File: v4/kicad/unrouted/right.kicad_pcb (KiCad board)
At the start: 2 copper layers, 160 x 118.6 mm, 72 parts

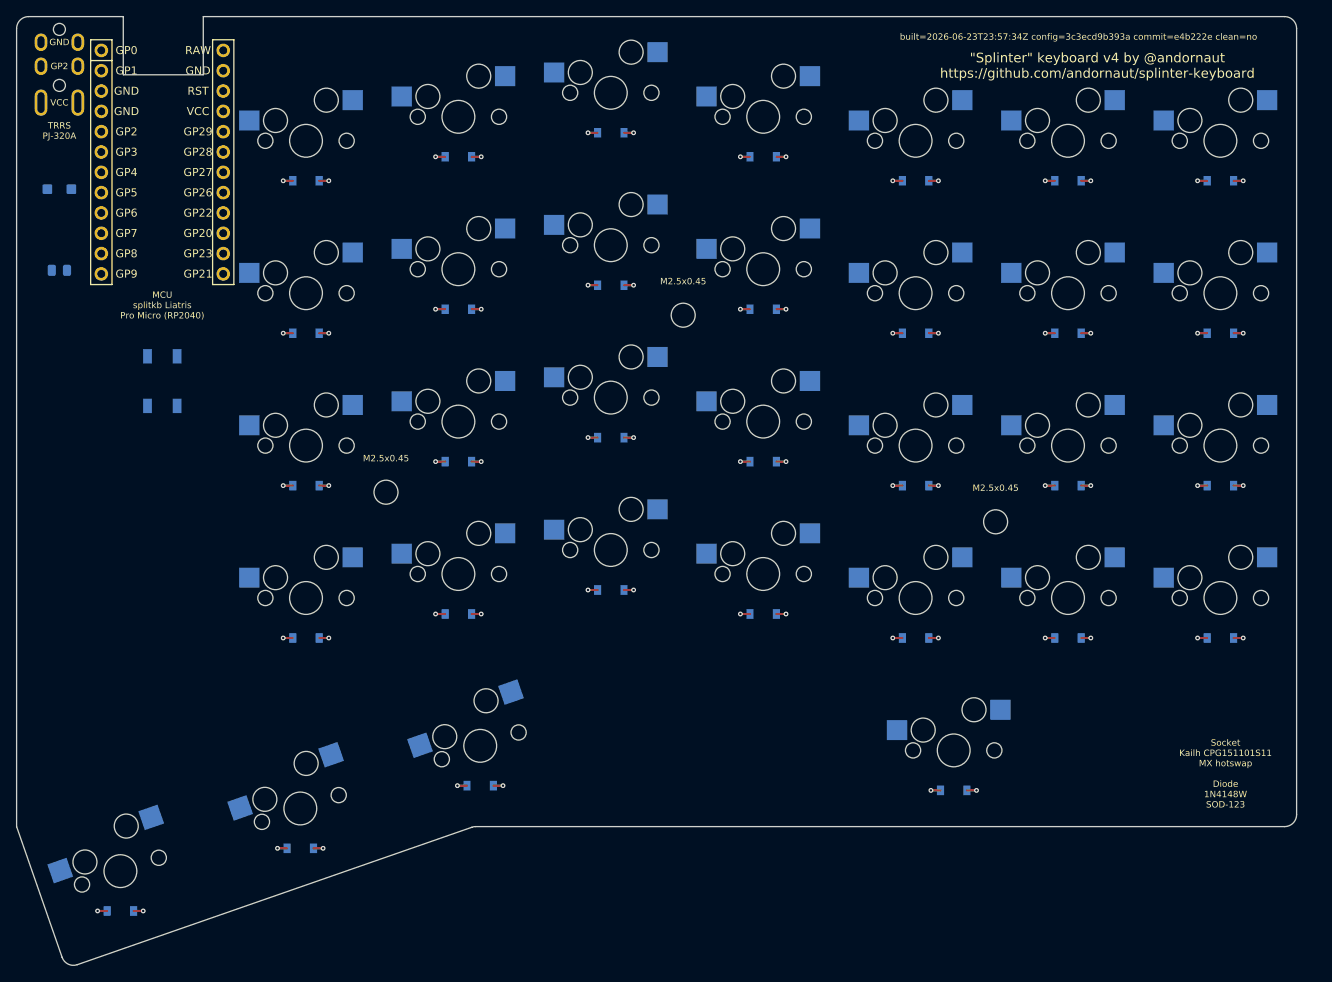
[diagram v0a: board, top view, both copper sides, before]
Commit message: v4: front-relative raw_pin_column, left-half nets on the partner pins
mcu_liatris now takes raw_pin_column: front_left | front_right instead of
left | right. The values name the PCB front because the MCU mounts on the
back, so the natural way to hold the board reverses the columns and the
bare left/right spelling silently assumed a frame. A stale left/right value
is rejected rather than reinterpreted.

The left half's matrix nets move to their socket-row partners (P4 -> P19,
P5 -> P18, and so on) so the net names and the silk labels name the pin
each net actually reaches. P2 stays put: QMK has one split.serial.pin, so
both halves must share it.

mcu_y seats the footprint body outline flush with the board top edge.

Regenerates unrouted/. routed/ is deliberately untouched and still carries
the wiring the boards were fabricated with, so validate:provenance and
validate:firmware both report it stale until it is re-routed.
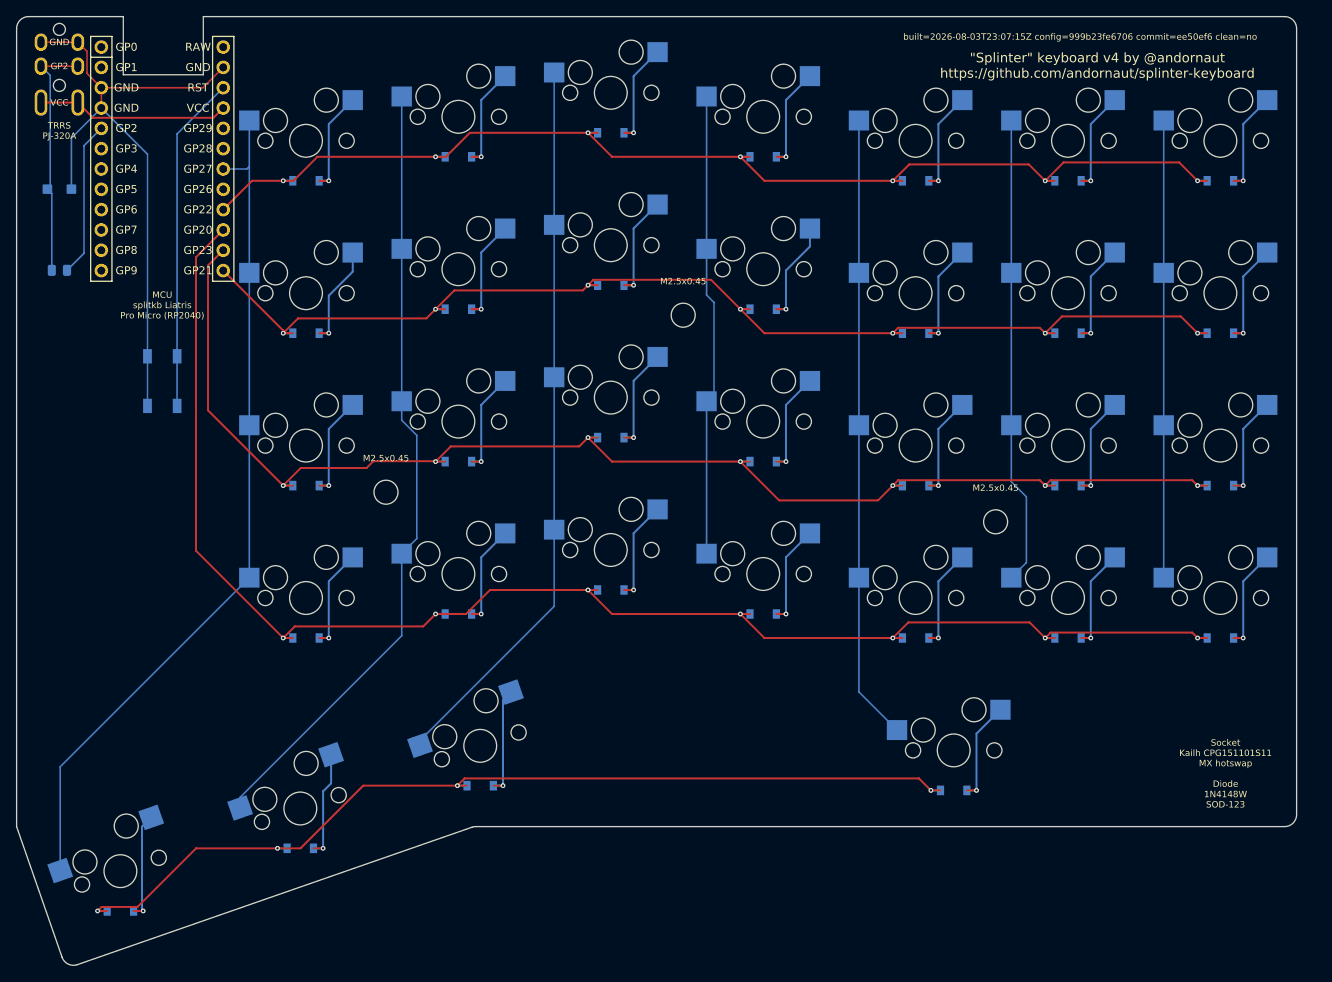
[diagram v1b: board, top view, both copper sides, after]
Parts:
- moved MCU1 0.42 mm to (148.5, 105.8)
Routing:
- net P14: track 16.8 -> 194.0 mm
- net P16: track 16.8 -> 172.9 mm
- net P10: track 16.8 -> 149.9 mm
- net P15: track 16.8 -> 146.3 mm
- net P9: track 9.60 -> 120.0 mm
- net P19: track 0.00 -> 106.9 mm
- net P8: track 0.00 -> 98.9 mm
- net P7: track 0.00 -> 91.0 mm
- net GND: track 0.00 -> 81.6 mm
- net P5: track 0.00 -> 78.2 mm
- net P4: track 0.00 -> 58.7 mm
- net P6: track 0.00 -> 57.9 mm
- net P3: track 0.00 -> 57.1 mm
- net RST: track 0.00 -> 42.2 mm
- net DATA_RAW: track 0.00 -> 31.0 mm
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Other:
- board text added: "built=2026-08-03T23:07:15Z config=999b23fe6706 commit=ee50ef6 clean=no"
- board text removed: "built=2026-06-23T23:57:34Z config=3c3ecd9b393a commit=e4b222e clean=no"

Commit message: v4: re-route both halves for the mirrored left-half pin mapping
Both halves are routed against the current config: the left half's matrix
nets on their MCU socket-row partners, and the MCU seated at the new mcu_y.
routed/ is re-derived from unrouted/ with the GND pour and teardrops (281
left, 296 right).

validate:provenance, validate:firmware, the fab DRC gate and validate:fab
all pass on all four boards. The routed/ .kicad_dru files land here for the
first time: apply-project-settings writes them per tier now.
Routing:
- net P3: track 57.1 -> 243.2 mm, vias 0 -> 1
- net P4: track 58.7 -> 225.0 mm, vias 0 -> 1
- net P5: track 78.2 -> 223.2 mm, vias 0 -> 1
- net P6: track 57.9 -> 183.2 mm, vias 0 -> 1
- net P7: track 91.0 -> 181.1 mm, vias 0 -> 1
- net P9: track 120.0 -> 194.2 mm
- net P8: track 98.9 -> 171.6 mm, vias 0 -> 1
- net P10: track 149.9 -> 142.5 mm
- net P15: track 146.3 -> 139.7 mm
- net P14: track 194.0 -> 190.6 mm
- net P16: track 172.9 -> 169.9 mm
- net mirror_five_mod: track 14.6 -> 13.2 mm, vias 1 -> 0
- net dash_upper: track 13.7 -> 12.5 mm, vias 1 -> 0
- net dash_num: track 13.7 -> 12.5 mm, vias 1 -> 0
- net dash_lower: track 13.7 -> 12.5 mm, vias 1 -> 0
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
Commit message: v4: strip the copper no route uses, in the pipeline
scripts/cleanup-tracks.py deletes dangling tracks and the vias they
strand, tracks buried in a pad of their own net, tracks laid over each
other, vias duplicating a via or a plated through-hole pad, and teardrops
left decorating nothing, then merges the segments an edit split.
copy:unrouted-to-routed runs it on each master after the GND pour, so the
fab source is cleaned every build. The working boards in unrouted/ keep
that copper, since a later reroute may pick it up.

scripts/pcb_copper.py holds the point-level connectivity test the cleanup
shares with add-gnd-zone.py, which now leaves the copper about to be
stripped out of its pour-layer score.

add-keepout-zones.py: weld the Edge.Cuts gap a stripped degenerate shape
leaves. KiCad closes a sub-micron gap silently but KiKit's ring
extraction matches endpoints exactly and aborts on it. One shape is
stripped per pass, because a weld moves the endpoints of the shapes still
to be tested.

Routed masters re-synced: DRC clean, 0 unconnected items, teardrops
unchanged (281 left, 296 right).
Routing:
- net P16: track 169.9 -> 178.3 mm
- net P15: track 139.7 -> 148.1 mm
- net P14: track 190.6 -> 199.0 mm
- net P10: track 142.5 -> 150.9 mm
- net P9: track 194.2 -> 199.0 mm
- net mirror_five_mod: track 13.2 -> 15.6 mm, vias 0 -> 1
- net P8: track 171.6 -> 169.5 mm
- net GND: track 82.0 -> 80.5 mm
- net dash_upper: track 12.5 -> 13.7 mm, vias 0 -> 1
- net dash_num: track 12.5 -> 13.7 mm, vias 0 -> 1
- net dash_lower: track 12.5 -> 13.7 mm, vias 0 -> 1
- net dash_home: track 12.5 -> 13.7 mm, vias 0 -> 1
- net zero_upper: track 12.5 -> 13.7 mm, vias 0 -> 1
- net zero_num: track 12.5 -> 13.7 mm, vias 0 -> 1
- net zero_lower: track 12.5 -> 13.7 mm, vias 0 -> 1
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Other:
- outline, holes or cut-outs redrawn
- board text added: "built=2026-08-04T01:57:26Z config=22a41bff1337 commit=3b96b62 clean=no"
- board text removed: "built=2026-08-03T23:07:15Z config=999b23fe6706 commit=ee50ef6 clean=no"

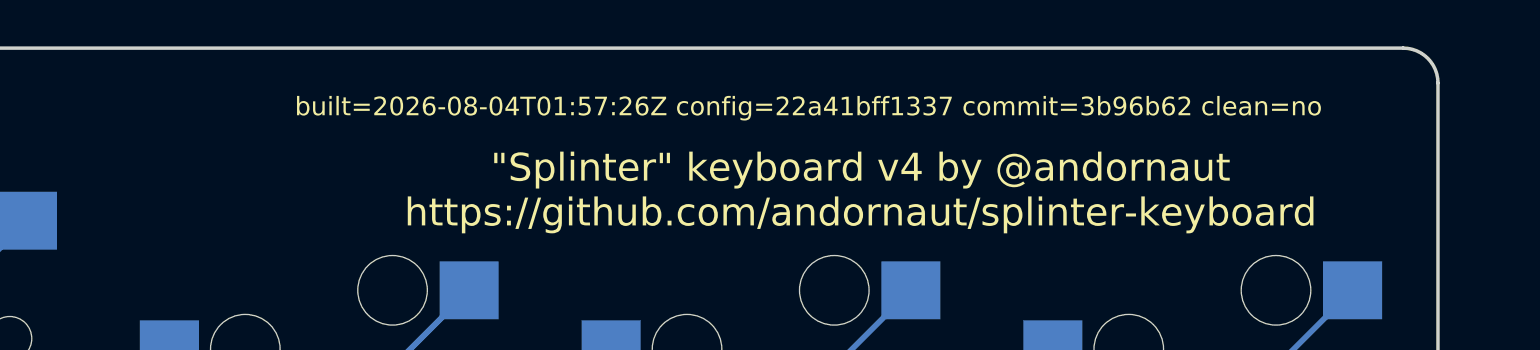
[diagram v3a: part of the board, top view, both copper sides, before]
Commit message: v4: rebuild the boards from a clean tree
Same geometry and routing; the provenance stamp now reads clean=yes
commit=ac19720, so the silkscreen and title block on the fabricated board
name the exact commit the gerbers came from.
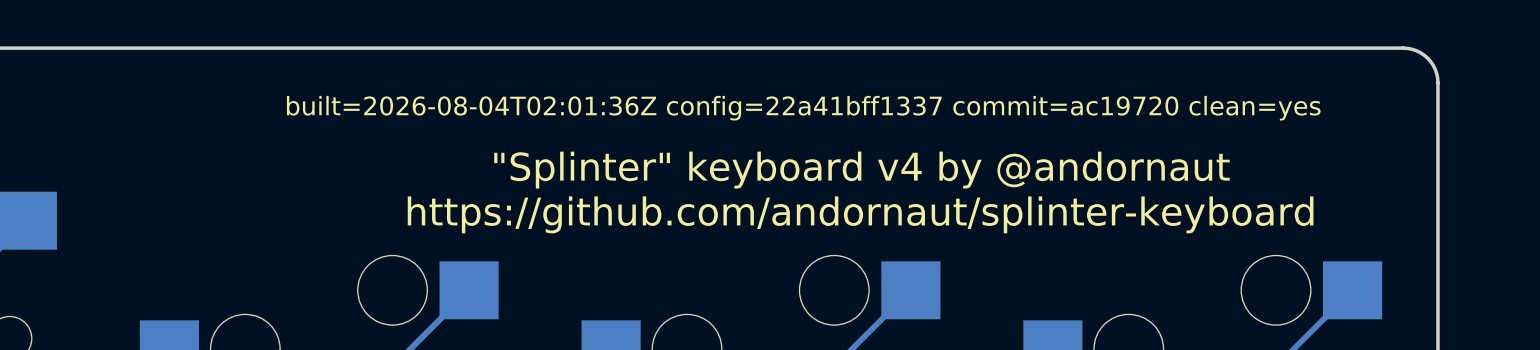
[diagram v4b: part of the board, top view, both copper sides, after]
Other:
- board text added: "built=2026-08-04T02:01:36Z config=22a41bff1337 commit=ac19720 clean=yes"
- board text removed: "built=2026-08-04T01:57:26Z config=22a41bff1337 commit=3b96b62 clean=no"

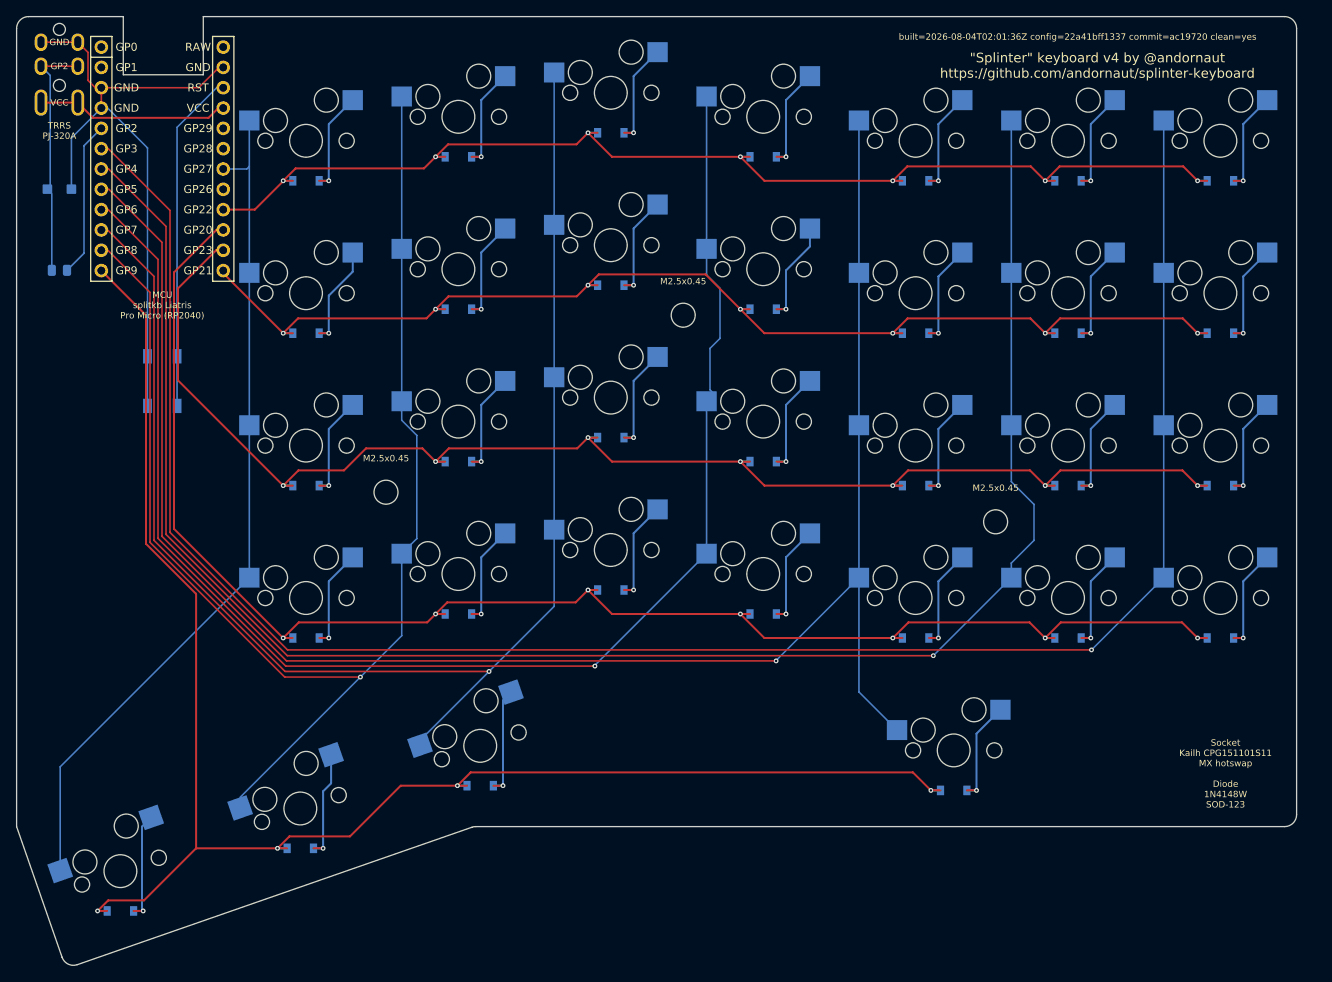
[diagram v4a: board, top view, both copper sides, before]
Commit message: v4: re-route the MCU exits, clean up to convergence
Route the header pins out straight for ~2.5mm before the first bend, so
KiCad can build a full-size teardrop instead of clipping it to a stub.
Teardrop copper is up from 296.2 to 302.1mm2 (left) and 315.2 to
323.9mm2 (right), and the count of clipped flares under 0.8mm2 is down
from 172 to 165 and 184 to 176.

cleanup-tracks.py now repeats its whole pass until one changes nothing,
capped at MAX_PASSES. The re-pour moved to the end of each pass, which
is what makes a repeat worth running: a track the old pour propped up
only reads as dangling once the pour has been re-flowed without it, and
the merge and the teardrop scan both run after the deletion fixpoint, so
nothing tested what they left. Every rule only removes copper, so a
changing pass strictly shrinks the board and the loop must converge; a
pass that still changes the board on the last allowed run is an error
and the board is left unsaved rather than half-cleaned.

Both halves converge in one changing pass. Routing is unchanged through
the pipeline round trip: 324/334 tracks, 36/38 vias, 281/297 teardrops,
0 unconnected.
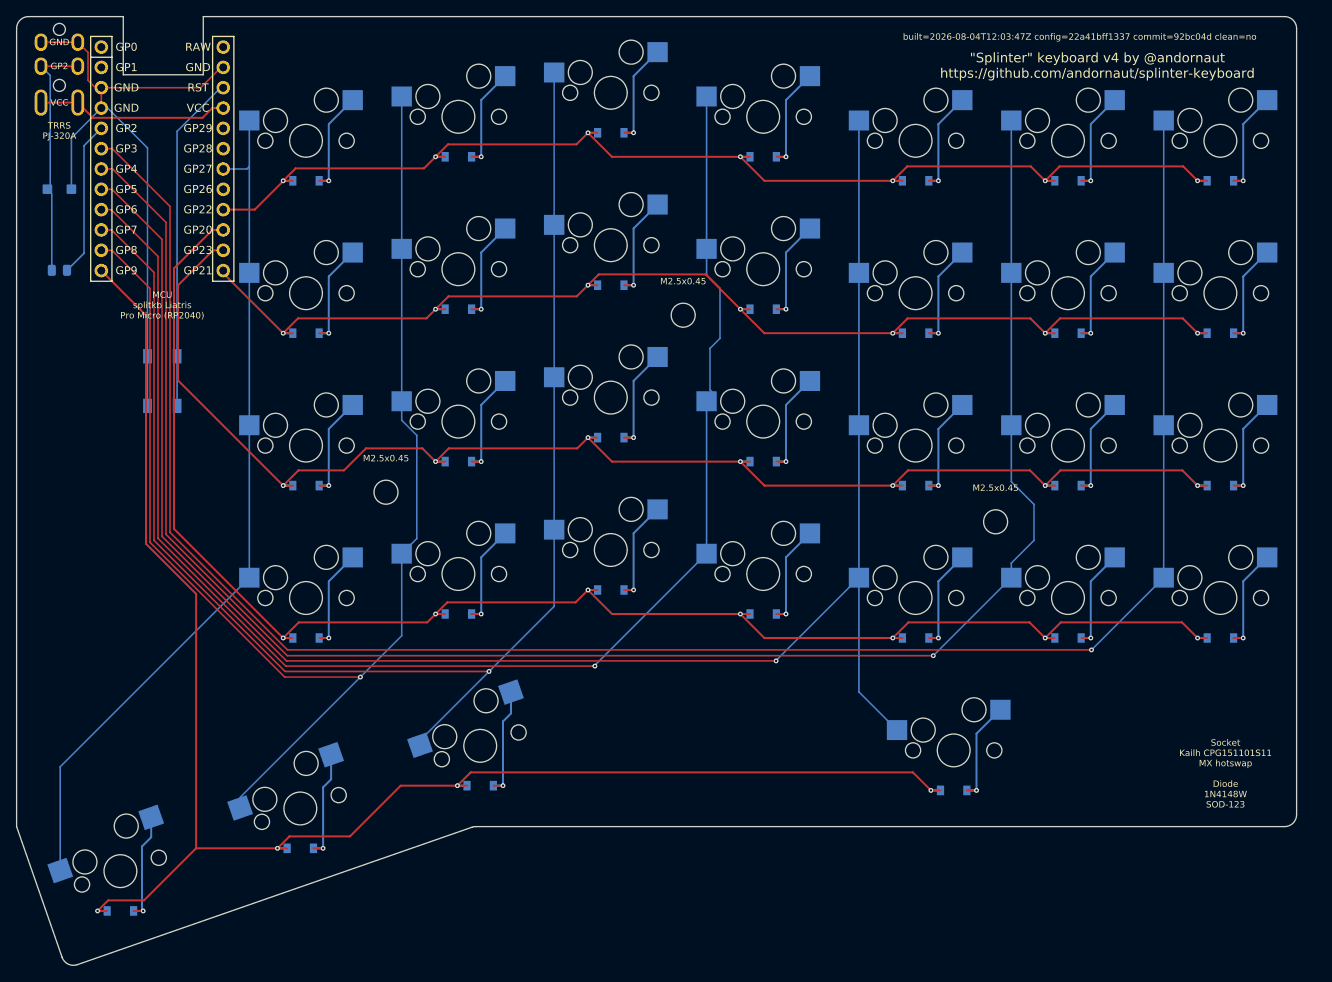
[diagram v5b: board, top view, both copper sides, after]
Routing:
- net mirror_three_mod: track 13.1 -> 14.5 mm
- net VCC: track 23.5 -> 24.1 mm
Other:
- board text added: "built=2026-08-04T12:03:47Z config=22a41bff1337 commit=92bc04d clean=no"
- board text removed: "built=2026-08-04T02:01:36Z config=22a41bff1337 commit=ac19720 clean=yes"

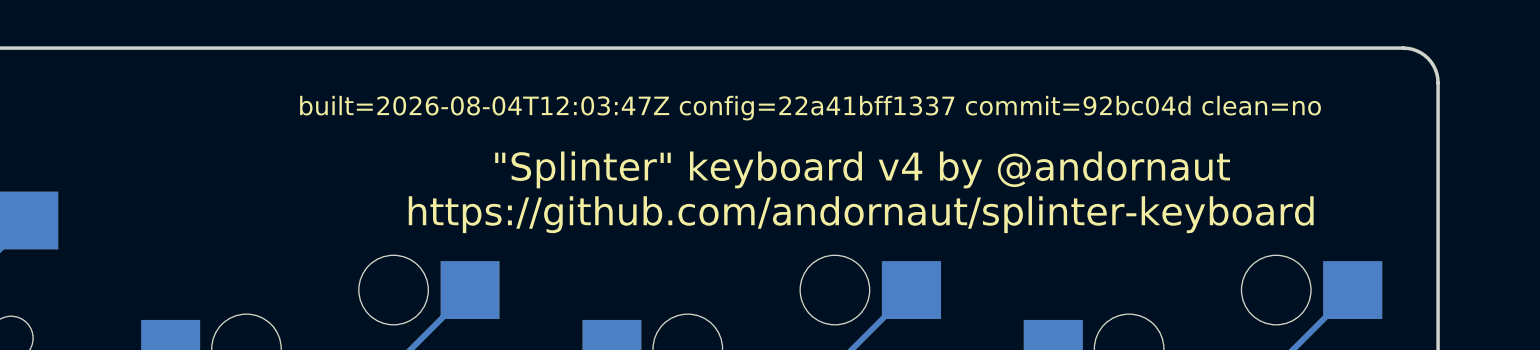
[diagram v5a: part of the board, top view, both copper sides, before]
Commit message: v4: rebuild the boards from a clean tree
Re-stamps all four boards with clean=yes commit=7aa9555, clearing the
two validate:fab non-clean-tree warnings. Copper is unchanged.
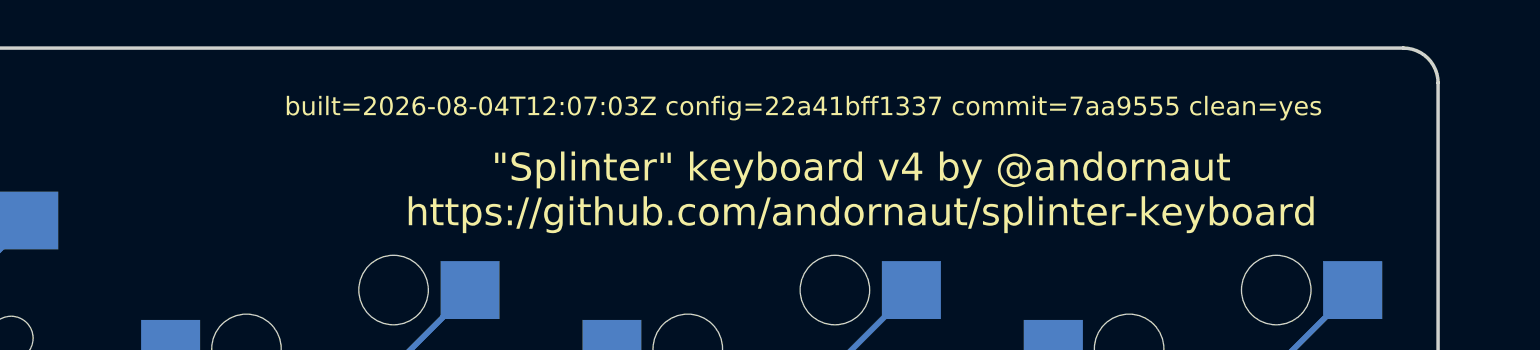
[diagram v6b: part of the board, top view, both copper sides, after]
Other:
- board text added: "built=2026-08-04T12:07:03Z config=22a41bff1337 commit=7aa9555 clean=yes"
- board text removed: "built=2026-08-04T12:03:47Z config=22a41bff1337 commit=92bc04d clean=no"
